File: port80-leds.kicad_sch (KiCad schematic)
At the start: 29 parts, among them U6001 SN74AC7541_VQFN, U6009 SN74AC7541_VQFN

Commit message: [#103910] Complete schematics
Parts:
- added D? (x2): LED_G_0603_LTST-C190GKT, antmicro-footprints:LED_0603_1608Metric_G, symbol antmicroLEDIndicationDiscrete:LED_G_0603_LTST-C190GKT
- added Q?: DMG1012T-7, antmicro-footprints:SOT-523, symbol antmicroTransistorsFETsMOSFETsSingle:DMG1012T-7
- added R? (x10): R_1k_0402, antmicro-footprints:R_0402_1005Metric, symbol antmicroResistors0402:R_1k_0402
- D6002, D6003, D6004, D6005, D6006, D6007, D6008, D6009: now fitted
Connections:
- net +3V3: now also R?.1, R?.1, R?.1, R?.1, R?.1, R?.1, R?.1, R?.1, R?.2, R?.2
- net 7SEG_L_A_R: no longer D6008.2 (A)
- net 7SEG_L_B_R: no longer D6002.2 (A)
- net 7SEG_L_C_R: no longer D6003.2 (A)
- net 7SEG_L_DP_R: no longer D6009.2 (A)
- net 7SEG_L_D_R: no longer D6004.2 (A)
- net 7SEG_L_E_R: no longer D6005.2 (A)
- net 7SEG_L_F_R: no longer D6006.2 (A)
- net 7SEG_L_G_R: no longer D6007.2 (A)
- net GND: now also Q?.2 (S); no longer D6002.1 (C), D6003.1 (C), D6004.1 (C), D6005.1 (C), D6006.1 (C), D6007.1 (C), D6008.1 (C), D6009.1 (C)
- new net: D?.2 (A), R?.1 (x2)
- new net: D6006.2 (A), R?.2
- new net: D6002.2 (A), R?.2
- new net: D6005.2 (A), R?.2
- new net: D6004.2 (A), R?.2
- new net: D?.1 (C), Q?.3 (D)
- new net: D6003.2 (A), R?.2
- new net: D6007.2 (A), R?.2
- new net: D6009.2 (A), R?.2
- new net: D6008.2 (A), R?.2
- new net DONE: Q?.1 (G)
- new net LED0: D6009.1 (C)
- new net LED1: D6007.1 (C)
- new net LED2: D6006.1 (C)
- new net LED3: D6005.1 (C)
- new net LED4: D6004.1 (C)
- new net LED5: D6003.1 (C)
- new net LED6: D6002.1 (C)
- new net LED7: D6008.1 (C)
- new net ~{INIT}: D?.1 (C)
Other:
- note removed: "Redundant LEDs"
- moved on the sheet: C6001, C6002, D6001, R6001, R6002, R6003, R6004, R6005, R6006, R6007, R6008, R6009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

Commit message: [#103910] Annotate schematics & Clean ERC
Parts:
- gave numbers to parts that had none: 13
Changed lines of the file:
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@@
 		(dnp no)
 		(fields_autoplaced yes)
-		(property "Reference" "D?"
+		(property "Reference" "D6011"
 			(at 113.03 129.54 90)
 			(show_name no)
@@
 			(project "machxo5-espi-debugger"
 				(path "/df391740-647e-4ab6-9dcd-d61184d66fe9/76679e57-0420-4874-b75d-368e938745be"
-					(reference "D?")
+					(reference "D6011")
 					(unit 1)
 				)
@@
 		(in_pos_files yes)
 		(dnp no)
-		(property "Reference" "R?"
+		(property "Reference" "R6024"
 			(at 177.038 134.366 0)
 			(show_name no)
@@
 			(project "machxo5-espi-debugger"
 				(path "/df391740-647e-4ab6-9dcd-d61184d66fe9/76679e57-0420-4874-b75d-368e938745be"
-					(reference "R?")
+					(reference "R6024")
 					(unit 1)
 				)
@@
 		(in_pos_files yes)
 		(dnp no)
-		(property "Reference" "R?"
+		(property "Reference" "R6020"
 			(at 177.038 114.046 0)
 			(show_name no)
@@
 			(project "machxo5-espi-debugger"
 				(path "/df391740-647e-4ab6-9dcd-d61184d66fe9/76679e57-0420-4874-b75d-368e938745be"
-					(reference "R?")
+					(reference "R6020")
 					(unit 1)
 				)
@@
 		(dnp no)
 		(fields_autoplaced yes)
-		(property "Reference" "R?"
+		(property "Reference" "R6017"
 			(at 92.71 123.19 90)
 			(show_name no)
@@
 			(project "machxo5-espi-debugger"
 				(path "/df391740-647e-4ab6-9dcd-d61184d66fe9/76679e57-0420-4874-b75d-368e938745be"
-					(reference "R?")
+					(reference "R6017")
 					(unit 1)
 				)
@@
 		(dnp no)
 		(fields_autoplaced yes)
-		(property "Reference" "R?"
+		(property "Reference" "R6018"
 			(at 113.03 123.19 90)
 			(show_name no)
@@
 			(project "machxo5-espi-debugger"
 				(path "/df391740-647e-4ab6-9dcd-d61184d66fe9/76679e57-0420-4874-b75d-368e938745be"
-					(reference "R?")
+					(reference "R6018")
 					(unit 1)
 				)
@@
 		(in_pos_files yes)
 		(dnp no)
-		(property "Reference" "R?"
+		(property "Reference" "R6022"
 			(at 177.038 124.206 0)
 			(show_name no)
@@
 			(project "machxo5-espi-debugger"
 				(path "/df391740-647e-4ab6-9dcd-d61184d66fe9/76679e57-0420-4874-b75d-368e938745be"
-					(reference "R?")
+					(reference "R6022")
 					(unit 1)
 				)
@@
 		(dnp no)
 		(fields_autoplaced yes)
-		(property "Reference" "D?"
+		(property "Reference" "D6010"
 			(at 92.71 129.54 90)
 			(show_name no)
@@
 			(project "machxo5-espi-debugger"
 				(path "/df391740-647e-4ab6-9dcd-d61184d66fe9/76679e57-0420-4874-b75d-368e938745be"
-					(reference "D?")
+					(reference "D6010")
 					(unit 1)
 				)
@@
 		(dnp no)
 		(fields_autoplaced yes)
-		(property "Reference" "Q?"
+		(property "Reference" "Q6001"
 			(at 86.36 138.43 0)
 			(show_name no)
@@
 			(project "machxo5-espi-debugger"
 				(path "/df391740-647e-4ab6-9dcd-d61184d66fe9/76679e57-0420-4874-b75d-368e938745be"
-					(reference "Q?")
+					(reference "Q6001")
 					(unit 1)
 				)
@@
 		(in_pos_files yes)
 		(dnp no)
-		(property "Reference" "R?"
+		(property "Reference" "R6021"
 			(at 177.038 119.126 0)
 			(show_name no)
@@
 			(project "machxo5-espi-debugger"
 				(path "/df391740-647e-4ab6-9dcd-d61184d66fe9/76679e57-0420-4874-b75d-368e938745be"
-					(reference "R?")
+					(reference "R6021")
 					(unit 1)
 				)
@@
 		(in_pos_files yes)
 		(dnp no)
-		(property "Reference" "R?"
+		(property "Reference" "R6026"
 			(at 177.038 144.526 0)
 			(show_name no)
@@
 			(project "machxo5-espi-debugger"
 				(path "/df391740-647e-4ab6-9dcd-d61184d66fe9/76679e57-0420-4874-b75d-368e938745be"
-					(reference "R?")
+					(reference "R6026")
 					(unit 1)
 				)
@@
 		(in_pos_files yes)
 		(dnp no)
-		(property "Reference" "R?"
+		(property "Reference" "R6025"
 			(at 177.038 139.446 0)
 			(show_name no)
@@
 			(project "machxo5-espi-debugger"
 				(path "/df391740-647e-4ab6-9dcd-d61184d66fe9/76679e57-0420-4874-b75d-368e938745be"
-					(reference "R?")
+					(reference "R6025")
 					(unit 1)
 				)
@@
 		(in_pos_files yes)
 		(dnp no)
-		(property "Reference" "R?"
+		(property "Reference" "R6023"
 			(at 177.038 129.286 0)
 			(show_name no)
@@
 			(project "machxo5-espi-debugger"
 				(path "/df391740-647e-4ab6-9dcd-d61184d66fe9/76679e57-0420-4874-b75d-368e938745be"
-					(reference "R?")
+					(reference "R6023")
 					(unit 1)
 				)
@@
 		(in_pos_files yes)
 		(dnp no)
-		(property "Reference" "R?"
+		(property "Reference" "R6019"
 			(at 177.038 108.966 0)
 			(show_name no)
@@
 			(project "machxo5-espi-debugger"
 				(path "/df391740-647e-4ab6-9dcd-d61184d66fe9/76679e57-0420-4874-b75d-368e938745be"
-					(reference "R?")
+					(reference "R6019")
 					(unit 1)
 				)

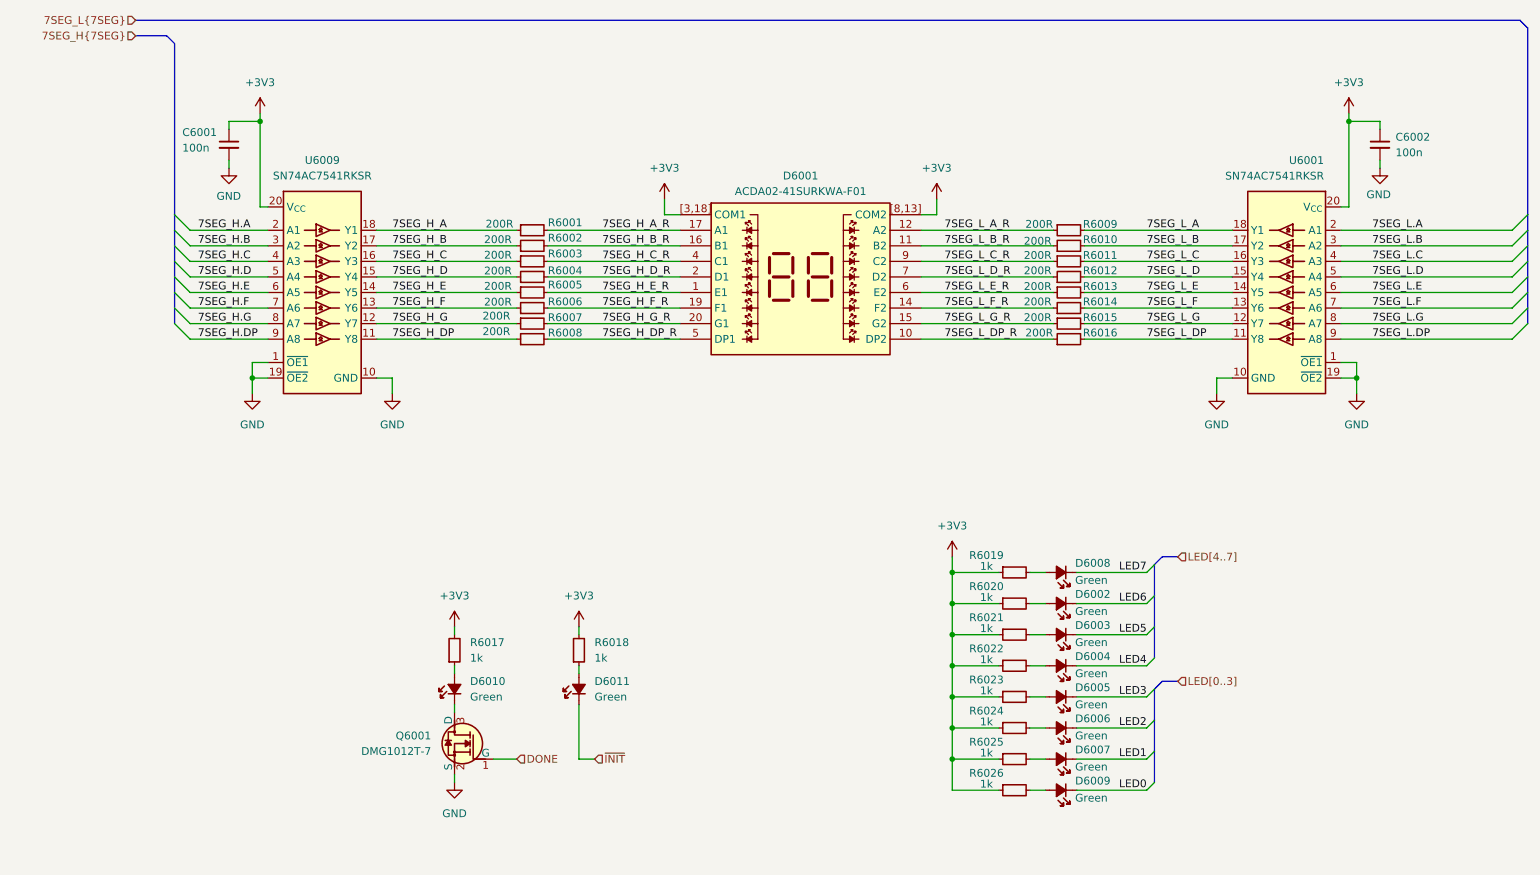
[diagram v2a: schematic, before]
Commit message: [#103953] sch/pcb: re-annotate components
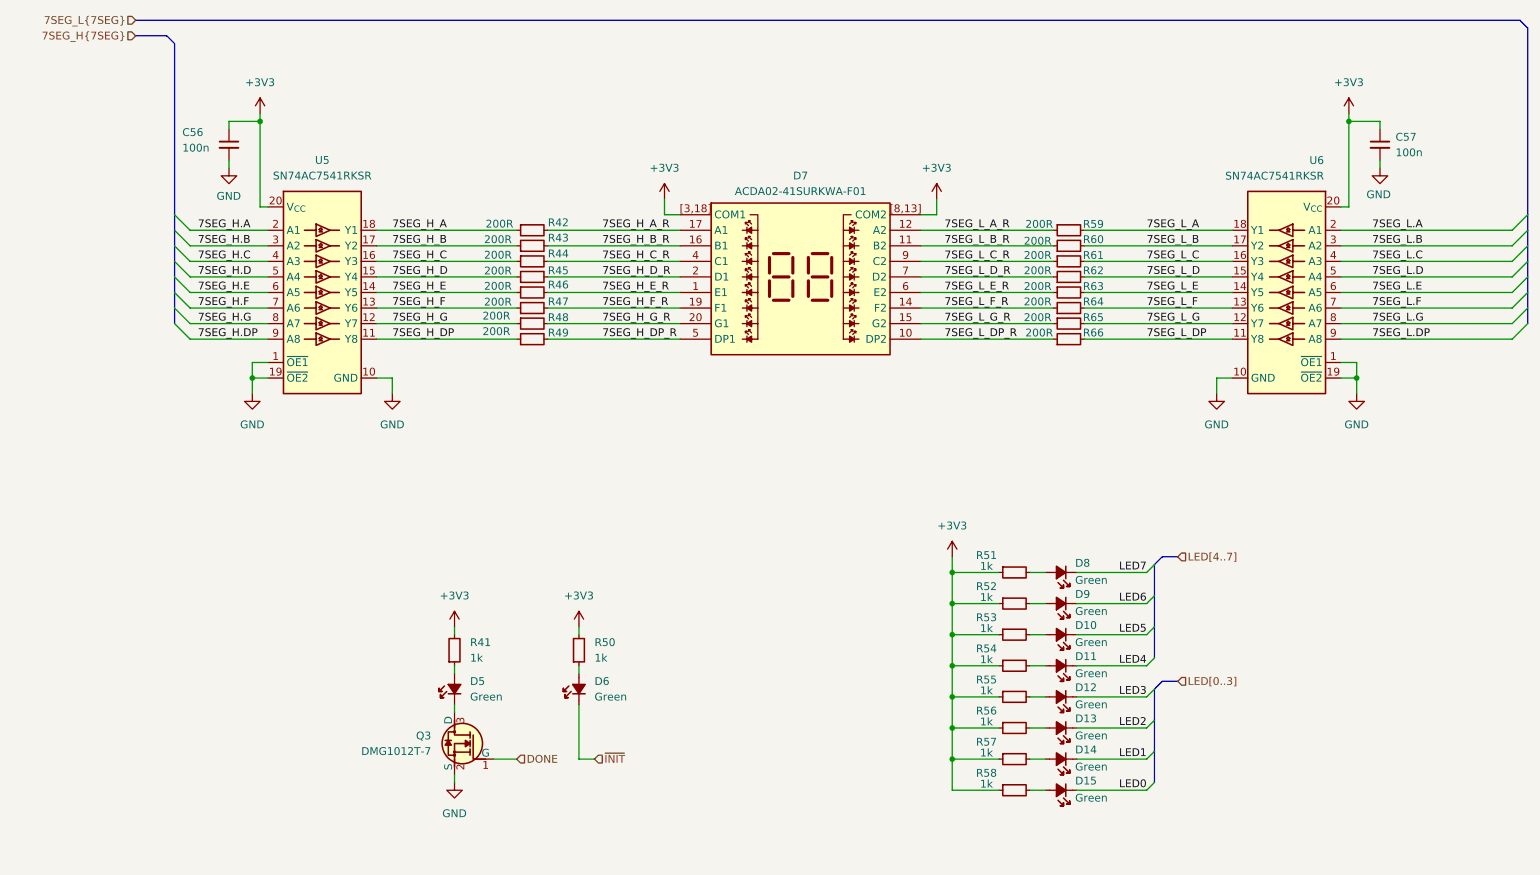
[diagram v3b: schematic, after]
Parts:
- renumbered C6001 to C56, C6002 to C57, D6003 to D10, D6004 to D11, D6005 to D12, D6006 to D13, D6007 to D14, D6009 to D15, D6010 to D5, D6011 to D6, D6001 to D7, D6008 to D8, D6002 to D9, Q6001 to Q3, R6017 to R41, R6001 to R42, R6002 to R43, R6003 to R44, R6004 to R45, R6005 to R46, R6006 to R47, R6007 to R48, R6008 to R49, R6018 to R50, R6019 to R51, R6020 to R52, R6021 to R53, R6022 to R54, R6023 to R55, R6024 to R56, R6025 to R57, R6026 to R58, R6009 to R59, R6010 to R60, R6011 to R61, R6012 to R62, R6013 to R63, R6014 to R64, R6015 to R65, R6016 to R66, U6009 to U5, U6001 to U6
